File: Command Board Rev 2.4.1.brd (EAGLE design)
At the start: 119.4 x 61 mm, 45 parts, among them IC1 PIC24FXXKA302_SPDIP, Q2-IRF510 IRF740

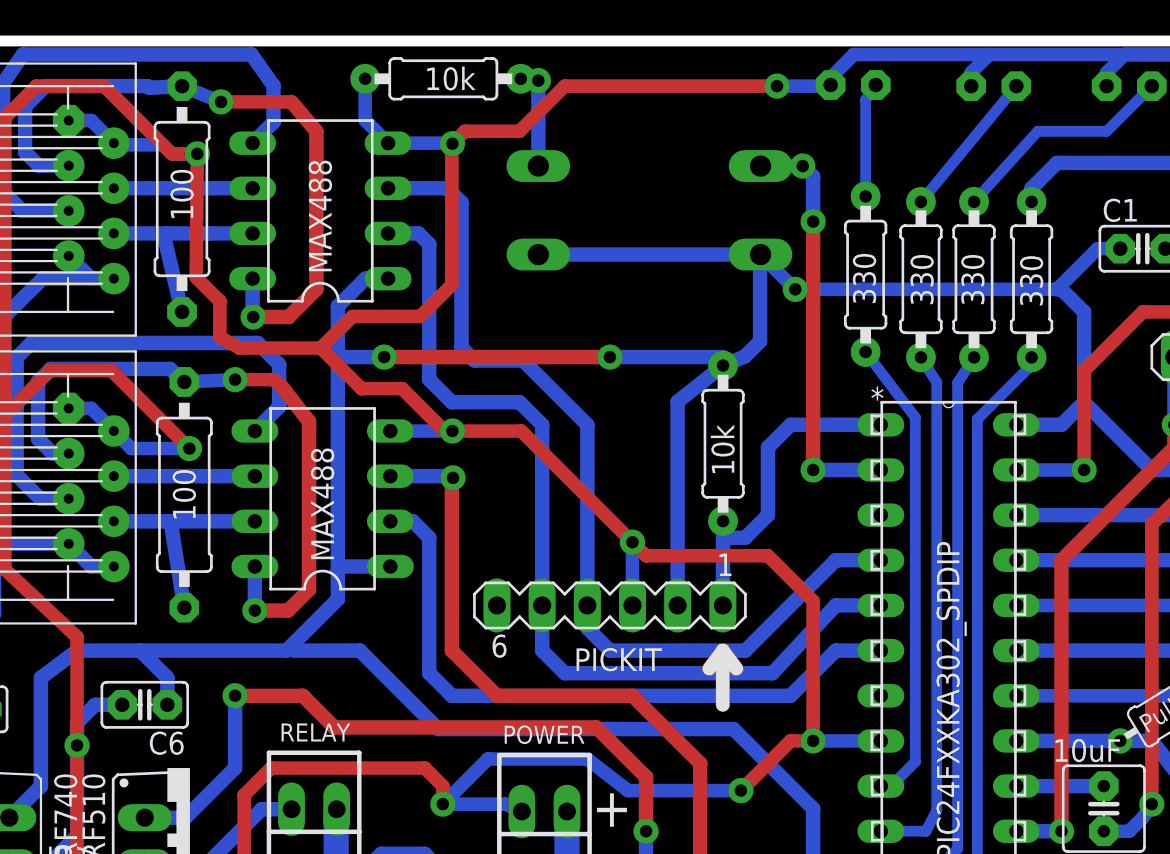
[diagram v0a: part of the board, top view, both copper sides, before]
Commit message: Remove 2.4, Add 2.4.1
Replaces 2.4 files with 2.4.1
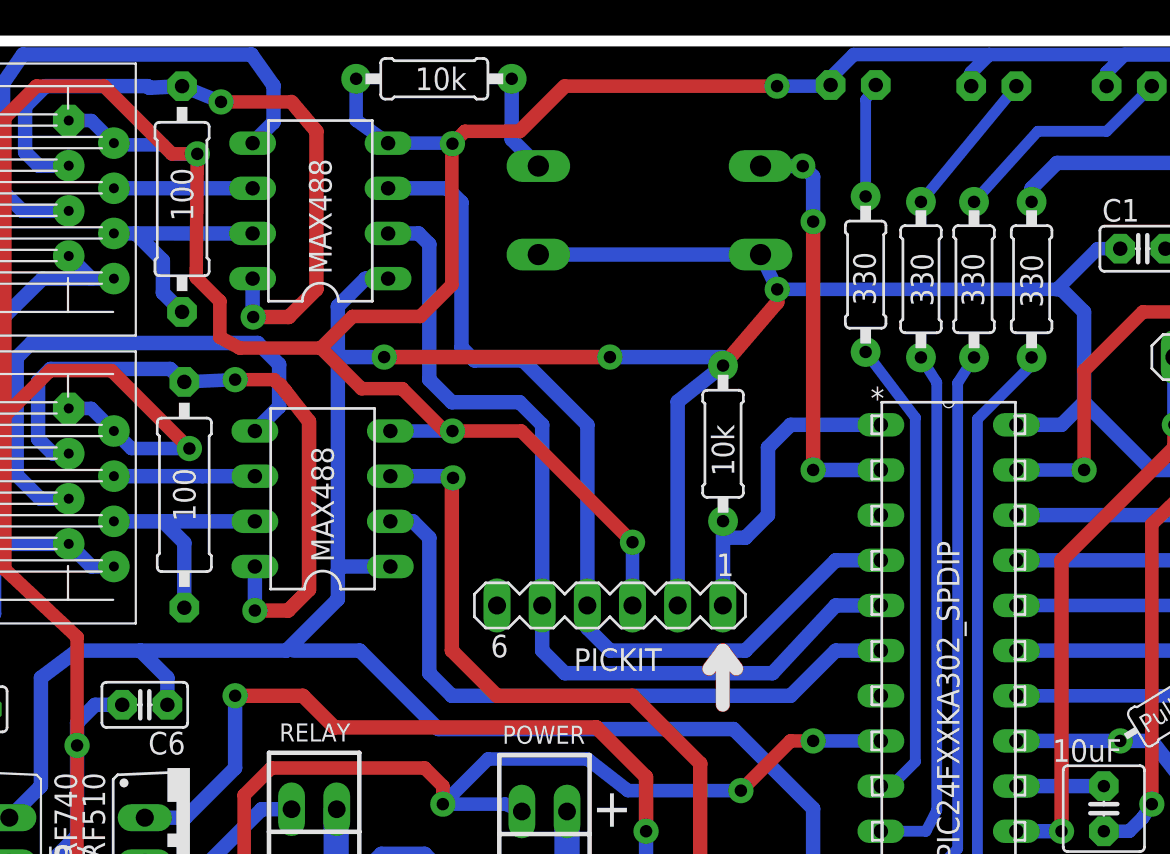
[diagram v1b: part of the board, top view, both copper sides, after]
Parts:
- moved R11 0.51 mm to (29.7, 58.8)
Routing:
- net GND: track 563.0 -> 544.0 mm
- net VCC: track 318.7 -> 317.1 mm, vias 7 -> 6
- net U2_B: track 12.4 -> 13.3 mm
- net U1_B: track 12.9 -> 13.4 mm
- net N$2: track 5.80 -> 5.53 mm, vias 1 -> 0
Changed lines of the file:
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@@
 <?xml version="1.0" encoding="utf-8"?>
 <!DOCTYPE eagle SYSTEM "eagle.dtd">
-<eagle version="7.4.0">
+<eagle version="7.7.0">
 <drawing>
 <settings>
@@
 <attribute name="NAME" x="107.696" y="3.302" size="1.016" layer="21" ratio="10" rot="R180"/>
 </element>
-<element name="R11" library="resistor" package="0207/10" value="10k" x="30.1625" y="58.83275" smashed="yes">
-<attribute name="VALUE" x="28.9179" y="58.19775" size="1.27" layer="21" ratio="10"/>
+<element name="R11" library="resistor" package="0207/10" value="10k" x="29.6545" y="58.83275" smashed="yes">
+<attribute name="VALUE" x="28.4099" y="58.19775" size="1.27" layer="21" ratio="10"/>
 </element>
 <element name="C1" library="adafruit" package="C025-025X050" value="0.1uF" x="69.342" y="49.276"/>
@@
 <wire x1="43.18" y1="29.21" x2="43.18" y2="40.671134375" width="0.8128" layer="16"/>
 <wire x1="43.18" y1="40.671134375" x2="45.7314" y2="42.701834375" width="0.8128" layer="16"/>
-<wire x1="45.7314" y1="42.701834375" x2="46.969034375" y2="43.222534375" width="0.8128" layer="16"/>
-<wire x1="46.969034375" y1="43.222534375" x2="47.8155" y2="44.069" width="0.8128" layer="16"/>
-<wire x1="47.8155" y1="44.069" x2="47.8155" y2="48.9204" width="0.8128" layer="16"/>
-<wire x1="47.8155" y1="48.9204" x2="47.8409" y2="48.9458" width="0.8128" layer="16"/>
 <contactref element="SLAVE1" pad="5"/>
 <contactref element="SLAVE2" pad="5"/>
@@
 <wire x1="68.072" y1="49.276" x2="66.802" y2="49.276" width="0.762" layer="16"/>
 <wire x1="66.802" y1="49.276" x2="64.516" y2="46.99" width="0.762" layer="16"/>
-<wire x1="64.516" y1="46.99" x2="49.7967" y2="46.99" width="0.762" layer="16"/>
-<wire x1="49.7967" y1="46.99" x2="47.8409" y2="48.9458" width="0.762" layer="16"/>
+<wire x1="64.516" y1="46.99" x2="48.7807" y2="46.99" width="0.762" layer="16"/>
+<wire x1="48.7807" y1="46.99" x2="47.8409" y2="48.9458" width="0.762" layer="16"/>
 <contactref element="C2" pad="1"/>
 <wire x1="109.982" y1="25.146" x2="111.76" y2="25.146" width="0.762" layer="16"/>
@@
 <wire x1="7.366" y1="25.146" x2="7.366" y2="19.05" width="0.8128" layer="16"/>
 <wire x1="7.366" y1="19.05" x2="5.588" y2="17.272" width="0.8128" layer="16"/>
-<via x="47.8155" y="48.9204" extent="1-16" drill="0.7" diameter="1.4224" shape="square"/>
-<via x="49.7967" y="46.99" extent="1-16" drill="0.7" diameter="1.4224" shape="square"/>
+<via x="48.7807" y="46.99" extent="1-16" drill="0.7" diameter="1.4224" shape="square"/>
 <via x="74.168" y="35.56" extent="1-16" drill="0.7" diameter="1.4224" shape="square"/>
 <via x="73.406" y="27.432" extent="1-16" drill="0.7" diameter="1.4224" shape="square"/>
@@
 <wire x1="73.406" y1="27.432" x2="73.914" y2="27.432" width="0.762" layer="16"/>
 <wire x1="73.914" y1="27.432" x2="75.438" y2="26.162" width="0.762" layer="16"/>
-<wire x1="45.72" y1="43.18" x2="45.7314" y2="42.701834375" width="0" layer="19" extent="16-16"/>
+<wire x1="48.7807" y1="46.99" x2="48.7807" y2="46.259134375" width="0.8128" layer="1"/>
+<wire x1="48.7807" y1="46.259134375" x2="45.7314" y2="42.701834375" width="0.8128" layer="1"/>
+<wire x1="45.72" y1="43.18" x2="45.7314" y2="42.701834375" width="0" layer="19" extent="1-16"/>
 <wire x1="24.0665" y1="46.0375" x2="24.13" y2="43.18" width="0" layer="19" extent="16-16"/>
 <wire x1="21.59" y1="26.67" x2="21.17725" y2="26.67" width="0" layer="19" extent="16-16"/>
@@
 <signal name="EMER_BTN_IN">
 <contactref element="IC1" pad="2"/>
-<contactref element="S1" pad="1"/>
-<wire x1="47.8409" y1="53.9242" x2="50.2158" y2="53.9242" width="0.8128" layer="16"/>
 <wire x1="50.2158" y1="53.9242" x2="50.8" y2="53.34" width="0.8128" layer="16"/>
 <wire x1="50.8" y1="53.34" x2="50.8" y2="50.8" width="0.8128" layer="16"/>
@@
 <wire x1="50.8" y1="36.83" x2="54.61" y2="36.83" width="0.8128" layer="16"/>
 <via x="50.2158" y="53.9242" extent="1-16" drill="0.7" diameter="1.4224" shape="square"/>
+<contactref element="S1" pad="1"/>
+<wire x1="47.8409" y1="53.9242" x2="50.2158" y2="53.9242" width="0.8128" layer="16"/>
 </signal>
 <signal name="GND">
@@
 <wire x1="26.89225" y1="55.21325" x2="30.51175" y2="55.21325" width="0.762" layer="16"/>
 <wire x1="30.51175" y1="55.21325" x2="30.51175" y2="55.1815" width="0.762" layer="16"/>
-<wire x1="25.6032" y1="58.83275" x2="25.6032" y2="56.5023" width="0.762" layer="16"/>
-<wire x1="25.6032" y1="56.5023" x2="26.89225" y2="55.21325" width="0.762" layer="16"/>
+<wire x1="25.0952" y1="58.83275" x2="25.0952" y2="56.5023" width="0.762" layer="16"/>
+<wire x1="25.0952" y1="56.5023" x2="26.89225" y2="55.21325" width="0.762" layer="16"/>
 <wire x1="8.93" y1="56.485" x2="10.2" y2="56.485" width="0.762" layer="16"/>
 <wire x1="10.2" y1="56.485" x2="11.47" y2="55.215" width="0.762" layer="16"/>
@@
 <wire x1="29.972" y1="18.034" x2="33.49625" y2="18.034" width="0.762" layer="16"/>
 <wire x1="33.49625" y1="18.034" x2="34.417" y2="17.62125" width="0.762" layer="16"/>
-<wire x1="50.8" y1="29.464" x2="48.26" y2="32.004" width="0.762" layer="1"/>
-<wire x1="48.26" y1="32.004" x2="41.402" y2="32.004" width="0.762" layer="1"/>
-<wire x1="41.402" y1="32.004" x2="40.64" y2="32.766" width="0.762" layer="1"/>
 <wire x1="110.77575" y1="34.00425" x2="104.29875" y2="34.06775" width="0.762" layer="16"/>
 <wire x1="104.29875" y1="34.06775" x2="104.14" y2="34.06775" width="0.762" layer="16"/>
@@
 <via x="48.768" y="58.42" extent="1-16" drill="0.7" diameter="1.4224" shape="square"/>
 <wire x1="48.768" y1="58.42" x2="36.83" y2="58.42" width="0.762" layer="1"/>
-<wire x1="36.83" y1="58.42" x2="34.29" y2="55.88" width="0.762" layer="1"/>
 <wire x1="34.29" y1="55.88" x2="31.21025" y2="55.88" width="0.762" layer="1"/>
 <wire x1="31.21025" y1="55.88" x2="30.51175" y2="55.1815" width="0.762" layer="1"/>
@@
 <wire x1="74.93" y1="58.42" x2="74.93" y2="59.436" width="0.8128" layer="16"/>
 <wire x1="74.93" y1="59.436" x2="75.692" y2="60.198" width="0.8128" layer="16"/>
-<wire x1="50.8" y1="21.59" x2="50.8" y2="29.464" width="0.762" layer="1"/>
 <contactref element="C1" pad="2"/>
 <wire x1="70.612" y1="49.276" x2="76.454" y2="49.276" width="0.762" layer="16"/>
@@
 <contactref element="C8" pad="2"/>
 <wire x1="80.01" y1="17.78" x2="85.09" y2="17.78" width="0.8128" layer="16"/>
+<wire x1="36.83" y1="58.42" x2="34.29" y2="55.88" width="0.8128" layer="1"/>
 </signal>
 <signal name="U2RX">
@@
 <contactref element="XCVR1" pad="7"/>
 <contactref element="R8" pad="1"/>
-<wire x1="11.47" y1="33.9425" x2="14.605" y2="33.9425" width="0.8128" layer="16"/>
+<wire x1="11.47" y1="33.9425" x2="14.224" y2="33.9425" width="0.8128" layer="16"/>
+<wire x1="14.224" y1="33.9425" x2="14.605" y2="33.9425" width="0.8128" layer="16"/>
 <wire x1="14.605" y1="33.9425" x2="19.3975" y2="33.9425" width="0.8128" layer="16"/>
 <wire x1="19.3975" y1="33.9425" x2="19.39925" y2="33.94075" width="0.8128" layer="16"/>
 <wire x1="14.6685" y1="33.879" x2="14.605" y2="33.9425" width="0.8128" layer="16"/>
-<wire x1="15.4305" y1="29.083" x2="14.6685" y2="33.879" width="0.8128" layer="16"/>
+<wire x1="15.4305" y1="29.083" x2="15.4305" y2="32.736" width="0.8128" layer="16"/>
+<wire x1="15.4305" y1="32.736" x2="14.224" y2="33.9425" width="0.8128" layer="16"/>
 </signal>
 <signal name="U1_A">
@@
 <contactref element="RJ1" pad="P$6"/>
 <contactref element="R9" pad="1"/>
-<wire x1="11.47" y1="50.135" x2="14.44625" y2="50.135" width="0.8128" layer="16"/>
-<wire x1="14.44625" y1="50.135" x2="16.764" y2="50.135" width="0.8128" layer="16"/>
-<wire x1="16.764" y1="50.135" x2="19.27225" y2="50.13325" width="0.8128" layer="16"/>
-<wire x1="15.3035" y1="45.72" x2="14.2875" y2="49.97625" width="0.8128" layer="16"/>
-<wire x1="14.2875" y1="49.97625" x2="14.44625" y2="50.135" width="0.8128" layer="16"/>
+<wire x1="11.47" y1="50.135" x2="12.700078125" y2="50.134725" width="0.8128" layer="16"/>
+<wire x1="12.700078125" y1="50.134725" x2="19.27225" y2="50.13325" width="0.8128" layer="16"/>
+<wire x1="15.3035" y1="45.72" x2="14.224" y2="46.7995" width="0.8128" layer="16"/>
+<wire x1="14.224" y1="46.7995" x2="14.224" y2="48.610803125" width="0.8128" layer="16"/>
+<wire x1="14.224" y1="48.610803125" x2="12.700078125" y2="50.134725" width="0.8128" layer="16"/>
 </signal>
 <signal name="U2_Z">
@@
 <wire x1="82.55" y1="12.7" x2="85.09" y2="12.7" width="0.8128" layer="16"/>
 </signal>
-<signal name="N$2">
-<contactref element="S1" pad="2"/>
-<contactref element="R11" pad="2"/>
-<wire x1="35.3441" y1="53.9242" x2="35.3441" y2="58.73115" width="0.8128" layer="16"/>
-<wire x1="35.3441" y1="58.73115" x2="34.3535" y2="58.83275" width="0.8128" layer="16"/>
-<via x="35.3441" y="58.73115" extent="1-16" drill="0.7" diameter="1.4224" shape="square"/>
-</signal>
 <signal name="RELAY_CONTROL">
 <contactref element="IC1" pad="15"/>
@@
 <wire x1="45.72" y1="26.67" x2="46.482" y2="25.654" width="0.8128" layer="1"/>
 </signal>
+<signal name="N$2">
+<contactref element="S1" pad="2"/>
+<contactref element="R11" pad="2"/>
+<wire x1="33.8455" y1="58.83275" x2="33.8455" y2="55.4228" width="0.8128" layer="16"/>
+<wire x1="33.8455" y1="55.4228" x2="35.3441" y2="53.9242" width="0.8128" layer="16"/>
+</signal>
 </signals>
